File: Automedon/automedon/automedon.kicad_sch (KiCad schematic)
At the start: 10 parts, among them J1 701W-X2/03, J2 MS3100E24-22P, J3 PWM-02RMFS-TS7001, J4 PWM-02RMFS-TS7001, J45 PWM-02RMFS-TS7001, J5 Antenna, J6 WAP, SW1 RRS20F1ABLKREDBLK31P, SW3 KEYSWITCH_SPST

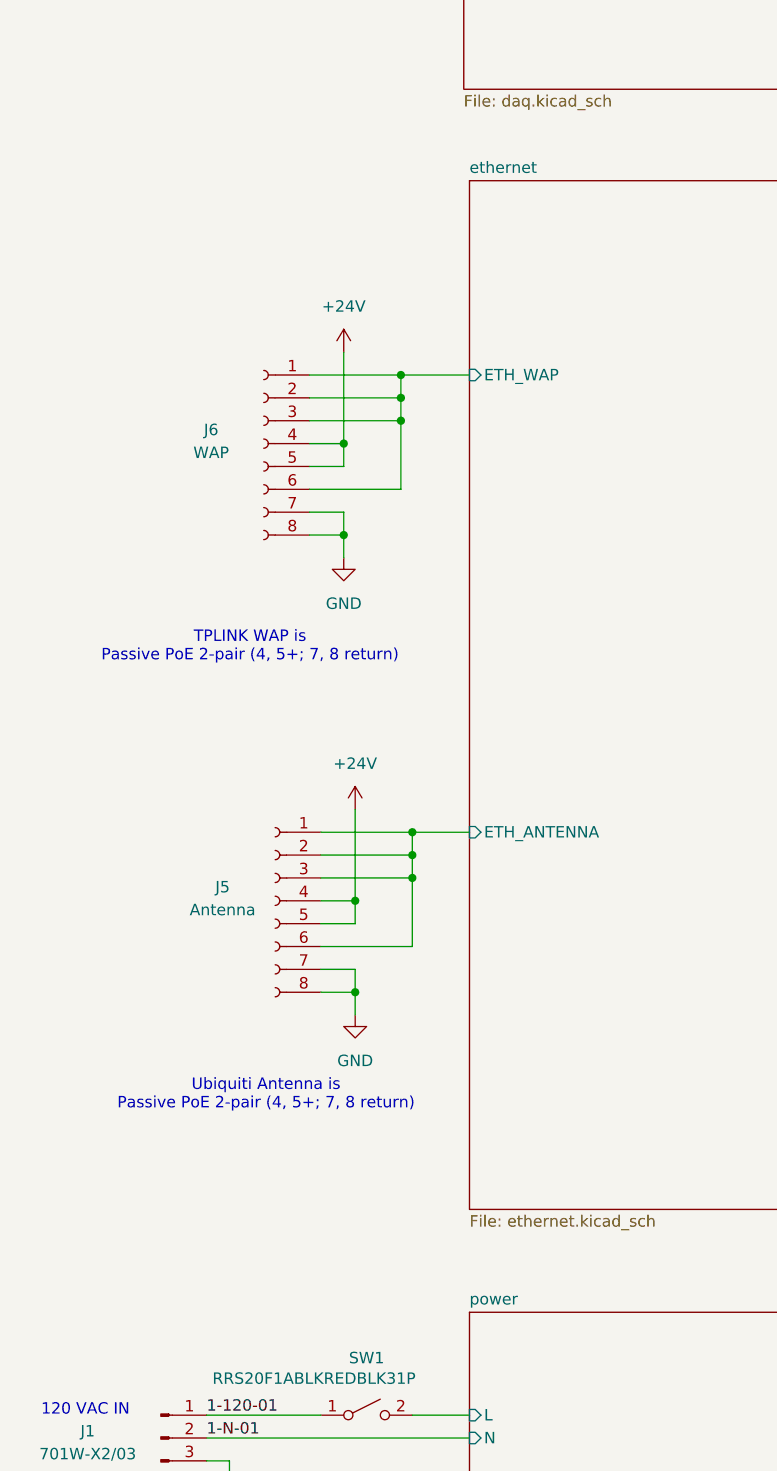
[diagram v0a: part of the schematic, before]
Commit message: Update eth ports
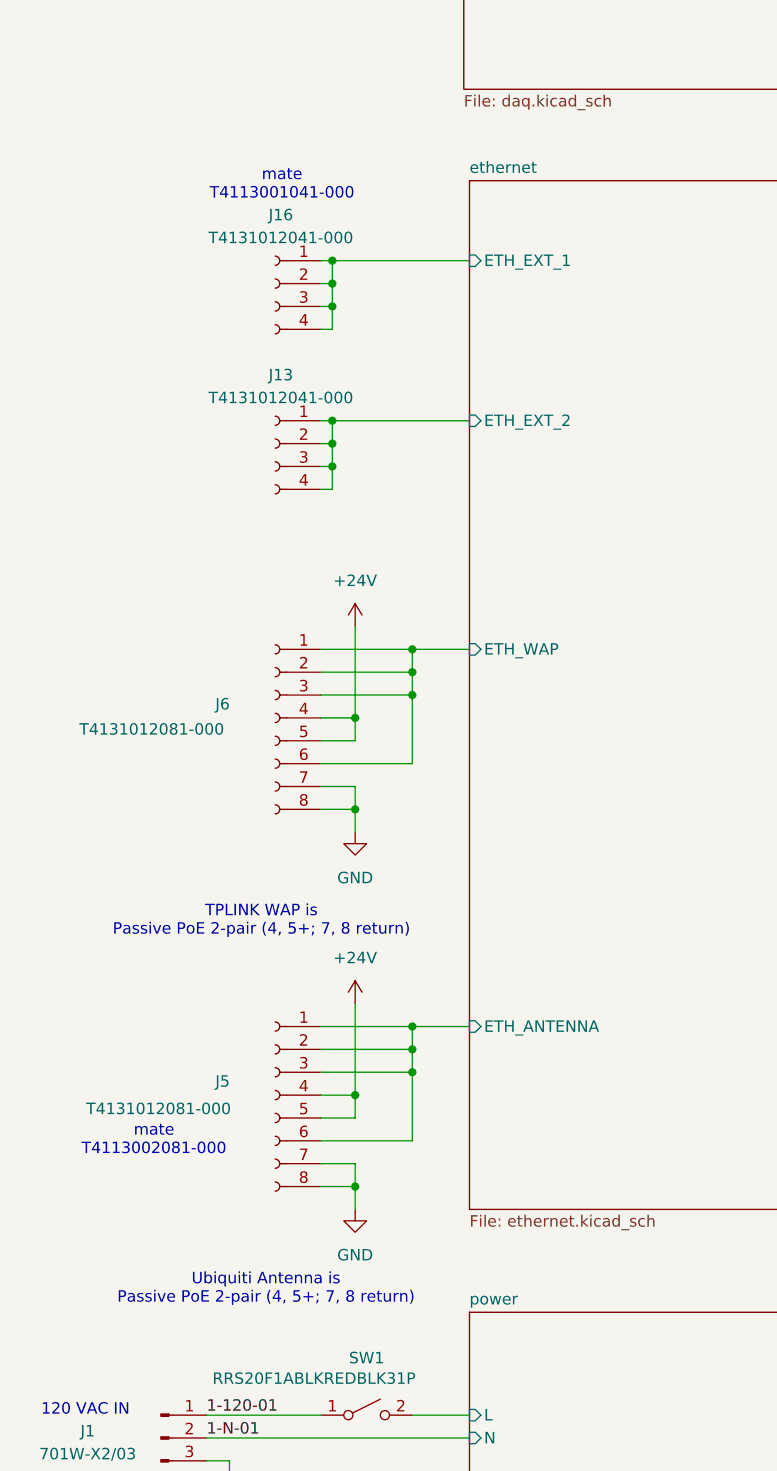
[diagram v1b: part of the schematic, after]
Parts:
- added J13, J16: T4131012041-000, symbol Connector:Conn_01x04_Socket
- J5: value Antenna -> T4131012081-000
- J6: value WAP -> T4131012081-000
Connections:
- new net ethernet/ETH_EXT_1: J16.1 (Pin_1), J16.2 (Pin_2), J16.3 (Pin_3), J16.4 (Pin_4)
- new net ethernet/ETH_EXT_2: J13.1 (Pin_1), J13.2 (Pin_2), J13.3 (Pin_3), J13.4 (Pin_4)
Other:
- sheet ethernet ports: added ETH_EXT_1, ETH_EXT_2; removed none
- note added: "mate T4113001041-000"
- note added: "mate T4113002081-000"
- moved on the sheet: J5, J6

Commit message: Update connector
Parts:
- J5, J6: value T4131012081-000 -> MSXS-08PFFP-SF7002
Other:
- note added: "mate MSXS-08BMMC-SL8002"
- note removed: "mate T4113002081-000"
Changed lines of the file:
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@@
 		)
 	)
-	(text "mate\nT4113002081-000"
+	(text "mate\nMSXS-08BMMC-SL8002"
 		(exclude_from_sim no)
 		(at 27.178 270.51 0)
@@
 			)
 		)
-		(property "Value" "T4131012081-000"
+		(property "Value" "MSXS-08PFFP-SF7002"
 			(at 27.686 266.954 0)
 			(effects
@@
 			)
 		)
-		(property "Value" "T4131012081-000"
+		(property "Value" "MSXS-08PFFP-SF7002"
 			(at 26.924 224.79 0)
 			(effects
